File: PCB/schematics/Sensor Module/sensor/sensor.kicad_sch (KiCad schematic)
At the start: 13 parts, among them IC1 EL5171ISZ-T7

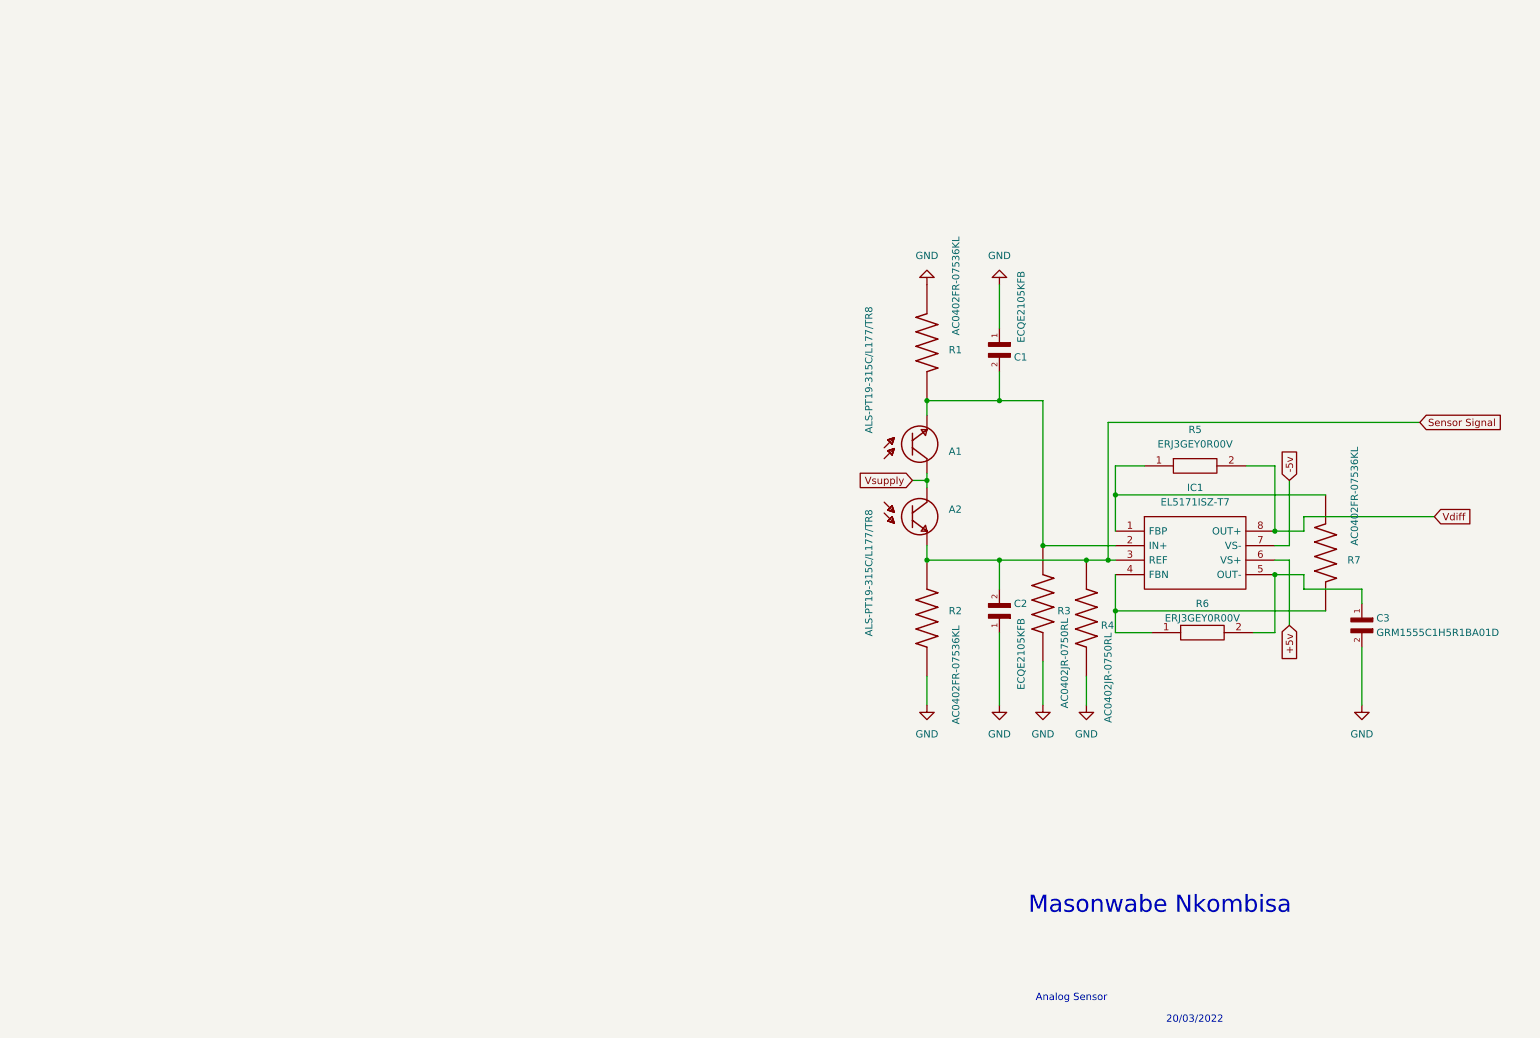
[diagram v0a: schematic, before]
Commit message: Modified pcb to reduced the gnd and 3.3v lines
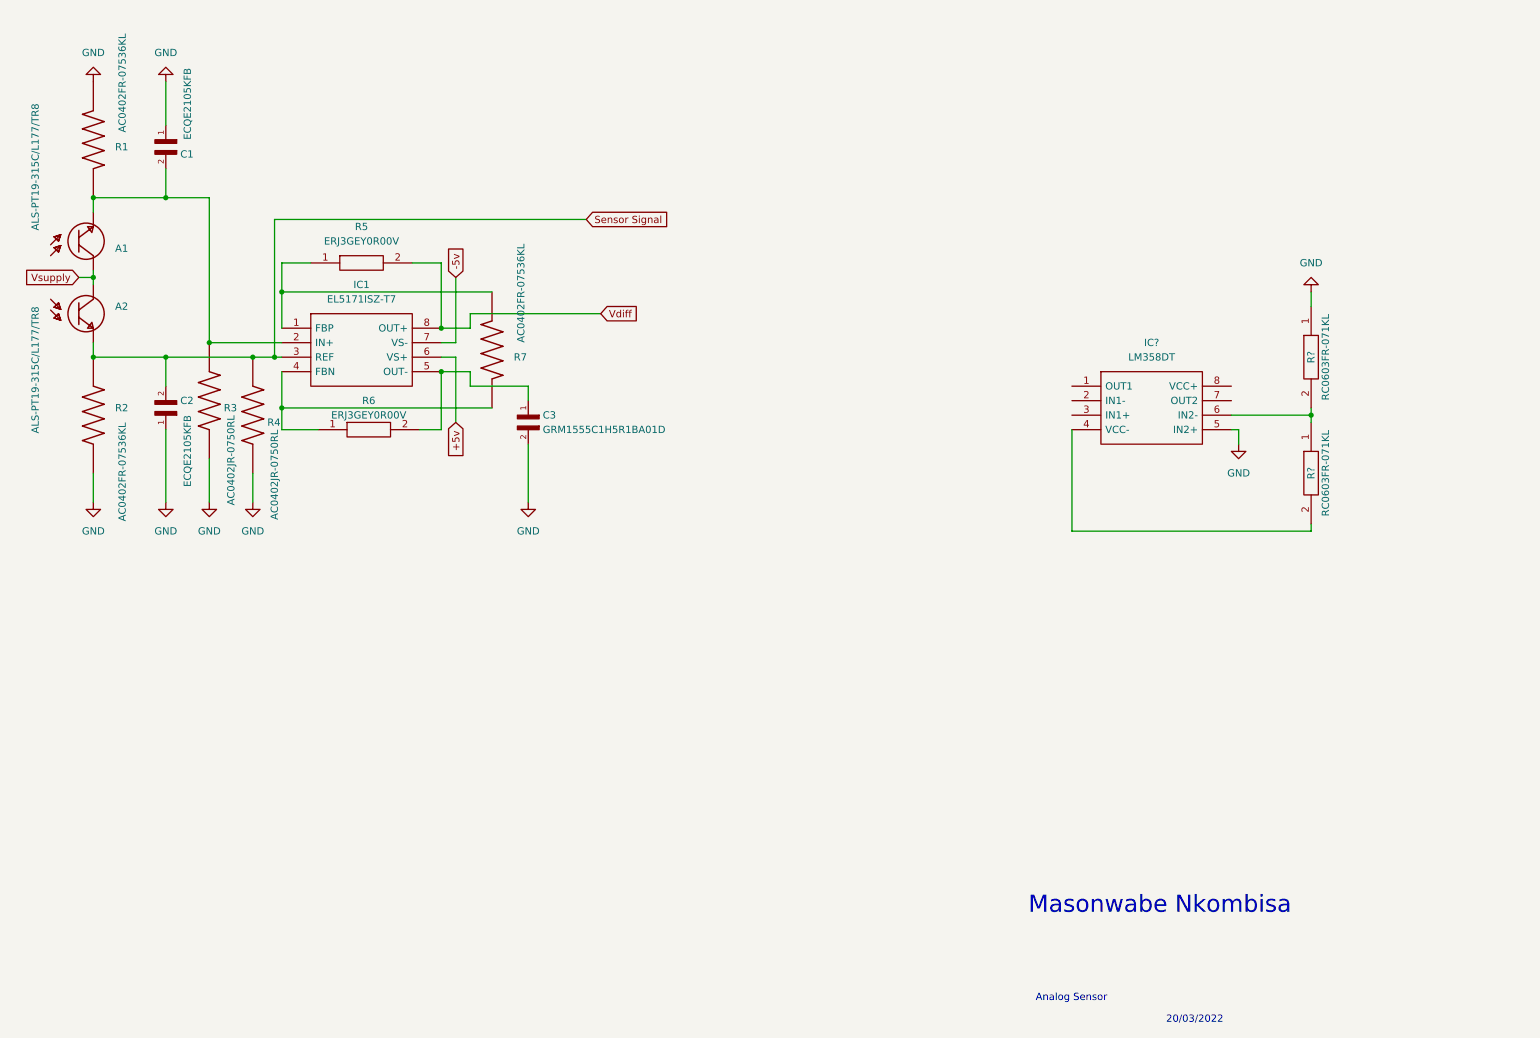
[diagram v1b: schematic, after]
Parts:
- added IC?: LM358DT, SamacSys_Parts:SOIC127P600X175-8N, symbol SamacSys_Parts:LM358DT
- added R? (x2): RC0603FR-071KL, SamacSys_Parts:RESC1608X55N, symbol SamacSys_Parts:RC0603FR-071KL
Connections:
- net GND: now also IC?.5 (IN2+), R?.1
- new net: IC?.6 (IN2-), R?.1, R?.2
- new net: IC?.4 (VCC-), R?.2
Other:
- moved on the sheet: A1, A2, C1, C2, C3, IC1, R1, R2, R3, R4, R5, R6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
